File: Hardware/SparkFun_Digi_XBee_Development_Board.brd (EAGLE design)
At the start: 45.7 x 63.5 mm, 150 parts, among them J4 QWIIC_RIGHT_ANGLE, Q2 3.1A/30V/105mΩ, U1 FSUSB30MUX_MSOP10, U2 AP63203, U3 ESD Diode, U4 MCP73831, U5 ESD Diode, U7 FT231XS

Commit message: Adds new FSUSB42 MUX switch
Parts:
- U6: value FSUSB30MUX_MSOP10 -> FSUSB42MUX
- renumbered U1 to U6
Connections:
- net D11/SDA: now also U6.7; no longer U6.2
- net DIRECT_D+: now also U6.9; no longer U6.3
- net DIRECT_D-: now also U6.8; no longer U6.7
- net DIRECT_SELECT: now also U6.2; no longer U6.1
- net GND: now also U6.10; no longer U6.9
- net N$3: now also U6.1; no longer U6.10
- net XBEE_D+/SDA: now also U6.3; no longer U6.4
- net XBEE_D-: now also U6.4; no longer U6.6
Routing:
- net XBEE_D-: track 21.7 -> 17.9 mm
- net GND: track 10.4 -> 8.95 mm, vias 78 -> 77
- net N$3: track 6.17 -> 7.44 mm
- net D11/SDA: track 54.9 -> 56.0 mm
- net DIRECT_D-: track 15.1 -> 14.2 mm, vias 2 -> 0
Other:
- board text added: "v13"
- board text removed: "v12"

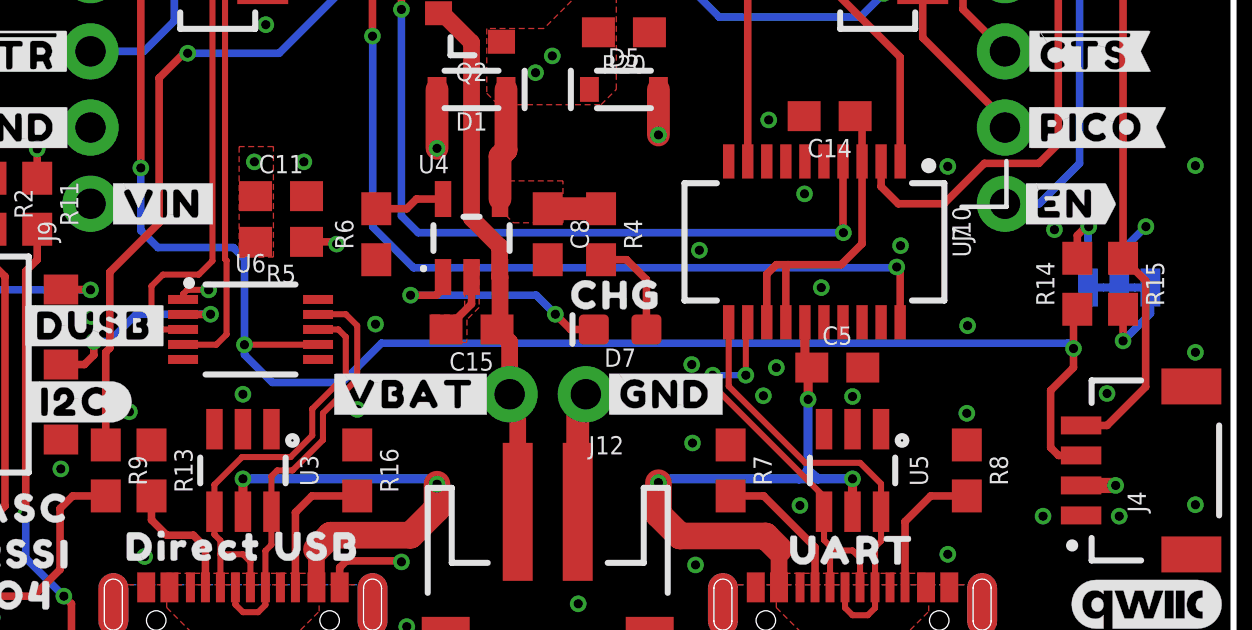
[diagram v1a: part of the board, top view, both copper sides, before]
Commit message: Adds text for USB calculation, nudges some things around for better pour
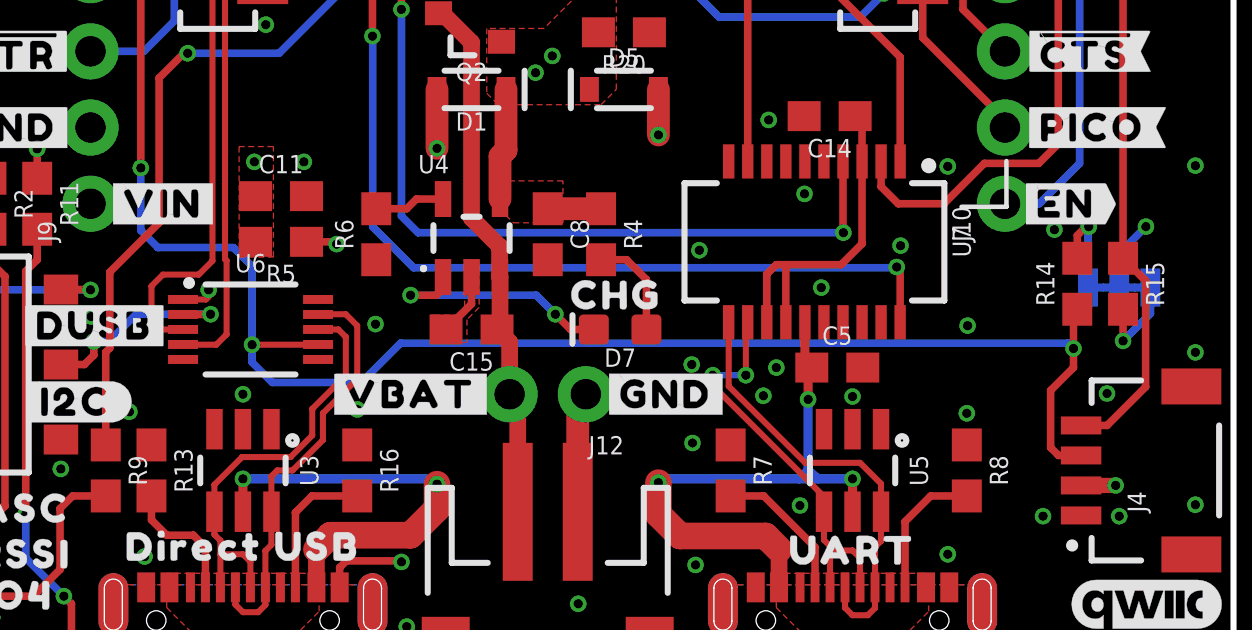
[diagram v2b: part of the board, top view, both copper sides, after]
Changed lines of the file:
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@@
 <layers>
 <layer number="1" name="Top" color="4" fill="1" visible="yes" active="yes"/>
-<layer number="2" name="Route2" color="23" fill="1" visible="yes" active="yes"/>
-<layer number="15" name="Route15" color="39" fill="1" visible="yes" active="yes"/>
+<layer number="2" name="Route2" color="23" fill="1" visible="no" active="yes"/>
+<layer number="15" name="Route15" color="39" fill="1" visible="no" active="yes"/>
 <layer number="16" name="Bottom" color="3" fill="1" visible="yes" active="yes"/>
 <layer number="17" name="Pads" color="26" fill="1" visible="yes" active="yes"/>
@@
 <layer number="37" name="tTest" color="7" fill="1" visible="no" active="yes"/>
 <layer number="38" name="bTest" color="7" fill="1" visible="no" active="yes"/>
-<layer number="39" name="tKeepout" color="4" fill="11" visible="yes" active="yes"/>
+<layer number="39" name="tKeepout" color="4" fill="11" visible="no" active="yes"/>
 <layer number="40" name="bKeepout" color="1" fill="11" visible="no" active="yes"/>
 <layer number="41" name="tRestrict" color="4" fill="10" visible="no" active="yes"/>
@@
 <layer number="115" name="ReferenceISLANDS" color="7" fill="1" visible="no" active="yes"/>
 <layer number="116" name="Patch_BOT" color="9" fill="4" visible="no" active="yes"/>
-<layer number="117" name="PM_Ref" color="26" fill="1" visible="no" active="yes"/>
+<layer number="117" name="PM_Ref" color="26" fill="1" visible="yes" active="yes"/>
 <layer number="118" name="Rect_Pads" color="7" fill="1" visible="no" active="yes"/>
-<layer number="119" name="PF_Ref" color="31" fill="1" visible="no" active="yes"/>
-<layer number="120" name="WFL_Ref" color="25" fill="1" visible="no" active="yes"/>
+<layer number="119" name="PF_Ref" color="31" fill="1" visible="yes" active="yes"/>
+<layer number="120" name="WFL_Ref" color="25" fill="1" visible="yes" active="yes"/>
 <layer number="121" name="_tsilk" color="7" fill="1" visible="no" active="yes"/>
 <layer number="122" name="_bsilk" color="7" fill="1" visible="no" active="yes"/>
@@
 <wire x1="9.2964" y1="20.2438" x2="9.2964" y2="27.5336" width="0.254" layer="1"/>
 <wire x1="9.2964" y1="27.5336" x2="7.62" y2="29.21" width="0.254" layer="1"/>
-<wire x1="12.7508" y1="17.2212" x2="12.3825" y2="17.5895" width="0.254" layer="16"/>
+<wire x1="13.0048" y1="16.9672" x2="12.3825" y2="17.5895" width="0.254" layer="16"/>
 <wire x1="40.64" y1="10.66" x2="39.886" y2="10.66" width="0.254" layer="1"/>
 <wire x1="39.886" y1="10.66" x2="39.624" y2="10.922" width="0.254" layer="1"/>
@@
 <wire x1="40.386" y1="15.406" x2="40.513" y2="15.533" width="0.254" layer="1"/>
 <wire x1="40.386" y1="14.224" x2="40.386" y2="15.406" width="0.254" layer="1"/>
-<wire x1="17.3228" y1="14.4018" x2="16.0147" y2="13.0937" width="0.254" layer="16"/>
-<wire x1="16.0147" y1="13.0937" x2="13.6779" y2="13.0937" width="0.254" layer="16"/>
-<wire x1="13.6779" y1="13.0937" x2="12.7508" y2="14.0208" width="0.254" layer="16"/>
-<wire x1="12.7508" y1="17.2212" x2="12.7508" y2="14.351" width="0.254" layer="16"/>
+<wire x1="17.9578" y1="14.4018" x2="16.6497" y2="13.0937" width="0.254" layer="16"/>
+<wire x1="16.6497" y1="13.0937" x2="13.6779" y2="13.0937" width="0.254" layer="16"/>
+<wire x1="13.6779" y1="13.0937" x2="13.0048" y2="13.7668" width="0.254" layer="16"/>
+<wire x1="13.0048" y1="16.9672" x2="13.0048" y2="14.351" width="0.254" layer="16"/>
 <wire x1="12.3825" y1="17.5895" x2="9.8679" y2="17.5895" width="0.254" layer="16"/>
 <wire x1="9.8679" y1="17.5895" x2="9.2964" y2="18.161" width="0.254" layer="16"/>
@@
 <via x="40.386" y="14.224" extent="1-16" drill="0.3048"/>
 <wire x1="40.386" y1="14.224" x2="40.2082" y2="14.4018" width="0.254" layer="16"/>
-<wire x1="40.2082" y1="14.4018" x2="17.3228" y2="14.4018" width="0.254" layer="16"/>
+<wire x1="40.2082" y1="14.4018" x2="17.9578" y2="14.4018" width="0.254" layer="16"/>
 <contactref element="U6" pad="7"/>
-<via x="12.7508" y="14.351" extent="1-16" drill="0.3048"/>
+<via x="13.0048" y="14.351" extent="1-16" drill="0.3048"/>
 <wire x1="15.204" y1="14.359" x2="15.196" y2="14.351" width="0.2032" layer="1"/>
-<wire x1="15.196" y1="14.351" x2="12.7508" y2="14.351" width="0.2032" layer="1"/>
-<wire x1="12.7508" y1="14.0208" x2="12.7508" y2="14.351" width="0.254" layer="16"/>
+<wire x1="15.196" y1="14.351" x2="13.0048" y2="14.351" width="0.2032" layer="1"/>
+<wire x1="13.0048" y1="13.7668" x2="13.0048" y2="14.351" width="0.254" layer="16"/>
 </signal>
 <signal name="D1/SCL">
@@
 <wire x1="15.748" y1="17.78" x2="14.82" y2="17.78" width="0.254" layer="1"/>
 <contactref element="U6" pad="1"/>
-<wire x1="10.8458" y1="16.1798" x2="10.704" y2="16.038" width="0.2032" layer="1"/>
-<wire x1="10.704" y1="15.859" x2="10.704" y2="16.038" width="0.2032" layer="1"/>
-<wire x1="10.8458" y1="16.1798" x2="11.557" y2="16.1798" width="0.2032" layer="1"/>
+<wire x1="11.557" y1="15.95" x2="11.466" y2="15.859" width="0.2032" layer="1"/>
+<wire x1="10.704" y1="15.859" x2="11.466" y2="15.859" width="0.2032" layer="1"/>
+<wire x1="11.557" y1="16.1798" x2="11.557" y2="15.95" width="0.2032" layer="1"/>
 <via x="11.557" y="16.1798" extent="1-16" drill="0.3048"/>
 <wire x1="11.557" y1="16.1798" x2="15.0114" y2="16.1798" width="0.2032" layer="2"/>

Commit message: Moves from 100 OHm to 0 OHm on VCC input for FUSB42
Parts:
- R5: value 100 -> 0
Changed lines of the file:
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@@
 <attribute name="VALUE" x="13.97" y="18.542" size="0.6096" layer="27" font="vector" ratio="20" align="top-center"/>
 </element>
-<element name="R5" library="SparkFun-Resistors" package="0603" value="100" x="13.97" y="17.78" smashed="yes" rot="R180">
+<element name="R5" library="SparkFun-Resistors" package="0603" value="0" x="13.97" y="17.78" smashed="yes" rot="R180">
 <attribute name="NAME" x="13.97" y="17.018" size="0.6096" layer="25" font="vector" ratio="20" rot="R180" align="bottom-center"/>
-<attribute name="PROD_ID" value="RES-07863" x="13.97" y="17.78" size="1.778" layer="27" font="vector" ratio="15" rot="R180" display="off"/>
-<attribute name="VALUE" x="13.97" y="18.542" size="0.6096" layer="27" font="vector" ratio="20" rot="R180" align="top-center"/>
+<attribute name="PROD_ID" value="RES-08609" x="13.97" y="17.78" size="1.778" layer="27" font="vector" ratio="15" rot="R180" display="off"/>
+<attribute name="VALUE" value="0" x="13.97" y="18.542" size="0.6096" layer="27" font="vector" ratio="20" rot="R180" align="top-center"/>
 </element>
 <element name="C12" library="SparkFun-Capacitors" package="0603" value="10pF" x="15.24" y="43.307" smashed="yes" rot="R270">
